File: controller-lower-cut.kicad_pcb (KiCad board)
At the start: 2 copper layers, 76.3 x 77 mm, 72 parts, among them J10 Phoenix MPT, J11 MicroFit_2x04, J12 Phoenix MPT, J13 MicroFit_2x04, J14 Phoenix MPT, J15 JST_B2B-XH, J16 MicroFit_2x04, J17 MLX_1x03, J18 MLX_1x03, J19 Phoenix MPT, J2 Conn_01x022_Male, J3 KYCON_KPJX-4S-S, J4 MicroFit_2x02, J5 24V/5A OUT, J7 Phoenix MPT, J9 Phoenix MPT, K1 OJS-SH-124HMF, Q1 BC847, Q2 IRFR5305TRPBF, Q3 BC857, Q4 BC847, Q5 BC857, U1 MAX5035BUSA

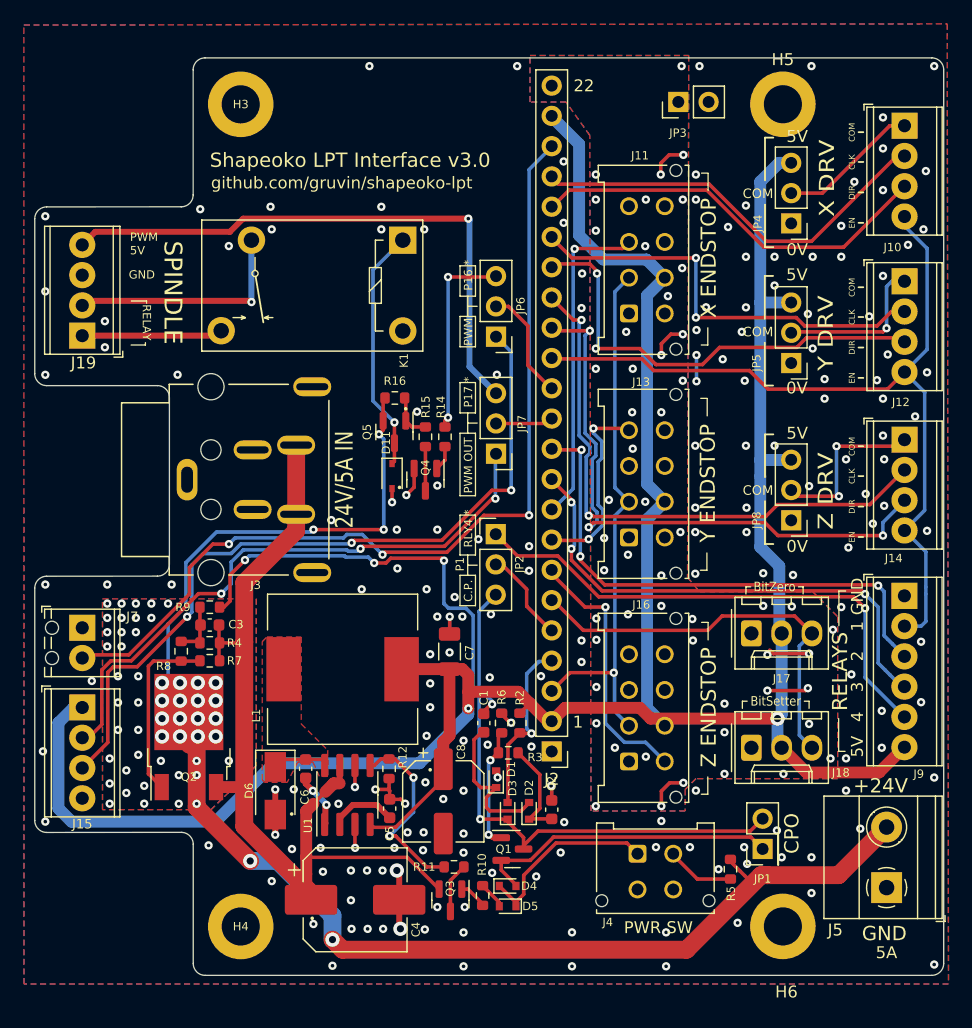
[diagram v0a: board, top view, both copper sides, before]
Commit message: v3.2 pre-production clean-up
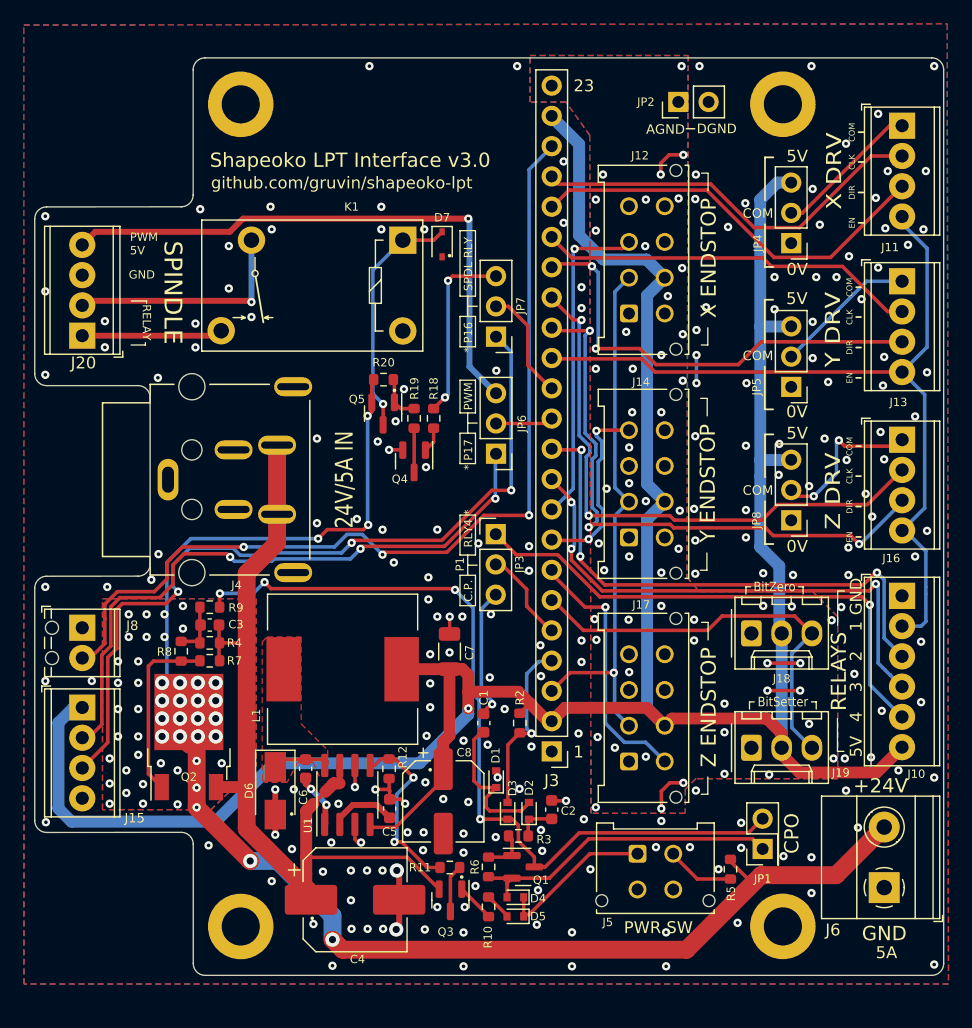
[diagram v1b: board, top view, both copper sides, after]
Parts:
- C1: value 10n/50V -> 100n/50V
- Q2: value IRFR5305TRPBF -> FDD5614P
- Q3: footprint Package_TO_SOT_SMD:SOT-23 -> -Project:SOT-23_DOT
- moved D7 19.9 mm to (70.9, 45.8)
- moved R6 12.1 mm to (74.8, 98.0), turned to -90 degrees
- moved R3 7.03 mm to (77.3, 95.4)
- moved JP5 2.00 mm to (100.2, 57.7)
- moved R20 1.81 mm to (66.0, 57.1)
- moved Q4 1.81 mm to (68.5, 64.0)
- moved Q5 1.81 mm to (66.0, 60.0)
- moved R18 1.81 mm to (70.2, 60.4)
- moved R19 1.81 mm to (68.5, 60.4)
- moved Q1 1.75 mm to (77.7, 98.0)
- moved JP4 1.66 mm to (100.2, 45.6)
- moved J4 1.60 mm to (57.0, 65.5)
- moved D4 1.15 mm to (77.0, 100.5), turned to 180 degrees
- moved R10 1.07 mm to (74.8, 101.3)
- moved D5 1.07 mm to (77.0, 102.2)
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- renumbered D11 to D7, H3 to H5, H4 to H6, H5 to H7, H6 to H8, J9 to J10, J10 to J11, J11 to J12, J12 to J13, J13 to J14, J14 to J16, J16 to J17, J17 to J18, J18 to J19, J19 to J20, J2 to J3, J3 to J4, J4 to J5, J5 to J6, J7 to J8, JP3 to JP2, JP2 to JP3, JP7 to JP6, JP6 to JP7, NT16 to NT22, NT17 to NT23, NT18 to NT24, NT33 to NT25, NT34 to NT26, NT35 to NT27, NT37 to NT28, R14 to R18, R15 to R19, R16 to R20
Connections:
- R6 pad 2: GND -> /Power/Q1_E
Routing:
- net /Power/Q1_B: track 10.2 -> 3.78 mm, vias 2 -> 0
- net Net-(C2-Pad1): track 8.61 -> 3.35 mm
- net GNDA: track 16.5 -> 12.3 mm, vias 53 -> 55
- net /Connectors & Jumpers/YCLK_IN: track 36.1 -> 32.0 mm, vias 2 -> 0
- net GND: track 27.4 -> 23.8 mm, vias 186 -> 199
- net /Connectors & Jumpers/X_P17_OUT: track 50.6 -> 53.6 mm
- net /Power/Q1_C: track 72.9 -> 70.0 mm
- net /Connectors & Jumpers/X_P16_OUT: track 64.8 -> 67.6 mm
- net Net-(D4-Pad1): track 16.2 -> 13.4 mm
- net +5V: track 174.5 -> 177.1 mm, vias 2 -> 1
- net /Connectors & Jumpers/STP_5V: track 31.8 -> 30.3 mm
- net /Connectors & Jumpers/RELAY3_IN: track 40.5 -> 42.0 mm
- net /Connectors & Jumpers/ESTOP_OUT: track 76.9 -> 78.3 mm
- net /Connectors & Jumpers/Y_COM: track 13.4 -> 11.9 mm, vias 1 -> 0
- net /Connectors & Jumpers/RELAY2_IN: track 42.5 -> 43.9 mm
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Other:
- outline, holes or cut-outs redrawn
- board text added: "* P16"
- board text added: "* P17"
- board text added: "23"
- board text added: "AGND"
- board text added: "DGND"
- board text added: "SPDL RLY"
- board text removed: "22"
- board text removed: "C"
- board text removed: "P16 *"
- board text removed: "P17 *"
- board text removed: "PWM OUT"
- board text removed: "TOOLING HOLE 1/3"

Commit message: more clean-up
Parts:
- moved J18 0.15 mm to (96.7, 78.4)
- moved J19 0.15 mm to (96.7, 88.0)
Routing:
- net GND: track 23.8 -> 21.4 mm, vias 199 -> 197
- net /Connectors & Jumpers/P16_IN: track 9.49 -> 8.81 mm
- net /Connectors & Jumpers/ZDIR_IN: track 49.7 -> 49.1 mm
- net GNDA: track 12.3 -> 12.8 mm, vias 55 -> 56
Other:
- board text added: "C"
- board text added: "Shapeoko LPT Interface v3.2"
- board text removed: "Shapeoko LPT Interface v3.0"

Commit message: more clean-up
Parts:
- added C10: 100n/50V, Capacitor_SMD:C_0603_1608Metric, F.Cu at (66.5, 127.8)
- added C11: 100n/50V, Capacitor_SMD:C_0603_1608Metric, F.Cu at (77.8, 144.4)
- added C12: 100n/50V, Capacitor_SMD:C_0603_1608Metric, F.Cu at (76.4, 127.7)
- added C9: 100n/50V, Capacitor_SMD:C_0603_1608Metric, F.Cu at (66.4, 159.1)
- added H1: MountingHole_Pad, MountingHole:MountingHole_3.2mm_M3_ISO14580_Pad, F.Cu at (110.0, 120.0)
- added H2: MountingHole_Pad, MountingHole:MountingHole_3.2mm_M3_ISO14580_Pad, F.Cu at (110.0, 189.0)
- added H3: MountingHole_Pad, MountingHole:MountingHole_3.2mm_M3_ISO14580_Pad, F.Cu at (54.0, 120.0)
- added H4: MountingHole_Pad, MountingHole:MountingHole_3.2mm_M3_ISO14580_Pad, F.Cu at (54.0, 189.0)
- added J1: Conn_01x06_Female, Connector_PinSocket_2.54mm:PinSocket_1x23_P2.54mm_Vertical, B.Cu at (136.1, 174.4)
- added J2: Conn_01x06_Female, Connector_PinSocket_2.54mm:PinSocket_1x23_P2.54mm_Vertical, B.Cu at (80.1, 174.4)
- added J7: DB25 FEMALE, Connector_Dsub:DSUB-25_Male_Horizontal_P2.77x2.84mm_EdgePinOffset7.70mm_Housed_MountingHolesOffset9.12mm, F.Cu at (55.6, 137.9)
- added NT1: NetTie_2, -Project:NetTie-2_SMD_Pad0.3mm, F.Cu at (74.6, 171.9)
- added R13: 1M, Resistor_SMD:R_0603_1608Metric, F.Cu at (73.3, 172.8)
- added R14: 330, Resistor_SMD:R_0603_1608Metric, F.Cu at (76.5, 167.2)
- added R15: 330, Resistor_SMD:R_0603_1608Metric, F.Cu at (76.5, 164.7)
- added R16: 330, Resistor_SMD:R_0603_1608Metric, F.Cu at (76.5, 162.2)
- added R17: 330, Resistor_SMD:R_0603_1608Metric, F.Cu at (76.5, 159.6)
- added R22: 330, Resistor_SMD:R_0603_1608Metric, F.Cu at (76.8, 121.5)
- added RN1: 1Kx4, Resistor_SMD:R_Array_Convex_4x0603, F.Cu at (64.6, 165.0)
- added RN2: 1Kx4, Resistor_SMD:R_Array_Convex_4x0603, F.Cu at (64.9, 123.1)
- added U2: 74HC245, Package_SO:SOIC-20W_7.5x12.8mm_P1.27mm, F.Cu at (71.2, 136.2)
- added U3: 74HC245, Package_SO:SOIC-20W_7.5x12.8mm_P1.27mm, F.Cu at (71.0, 150.8)
- added U4: ACSL-6310, Package_SO:SO-16_3.9x9.9mm_P1.27mm, F.Cu at (71.1, 164.0)
- added U5: ACSL-6310, Package_SO:SO-16_3.9x9.9mm_P1.27mm, F.Cu at (71.1, 123.3)
- added U6: USBLC6-2SC6, Package_TO_SOT_SMD:SOT-23-6, F.Cu at (111.0, 177.5)
- added U7: ADUM4160, Package_SO:SOIC-16W_7.5x10.3mm_P1.27mm, F.Cu at (114.8, 169.3)
- added U8: ATmega16U2-A, Package_QFP:TQFP-32_7x7mm_P0.8mm, F.Cu at (127.1, 169.2)
- added U9: ATmega328P-A, Package_QFP:TQFP-32_7x7mm_P0.8mm, F.Cu at (120.8, 150.9)
- JP1: value Jumper_2_Bridged -> Jumper_2
- JP4, JP5, JP8: value Jumper_3_Open -> Jumper_3
- moved R12 0.10 mm to (66.5, 89.8)
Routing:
- net +5VA: track 0.00 -> 179.6 mm, vias 0 -> 3
- net /LPT Interface/P1_IN: track 0.00 -> 63.5 mm, vias 0 -> 1
- net /LPT Interface/nCE_IN: track 0.00 -> 45.1 mm, vias 0 -> 4
- net GND2: track 0.00 -> 42.3 mm, vias 0 -> 44
- net /LPT Interface/P15_OUT: track 0.00 -> 28.3 mm
- net /LPT Interface/P7_IN: track 0.00 -> 23.0 mm
- net /LPT Interface/P6_IN: track 0.00 -> 21.1 mm
- net /LPT Interface/P5_IN: track 0.00 -> 19.3 mm
- net /LPT Interface/P4_IN: track 0.00 -> 17.5 mm
- net /LPT Interface/P3_IN: track 0.00 -> 15.7 mm
- net /LPT Interface/P11_OUT: track 0.00 -> 15.6 mm
- net /LPT Interface/P13_OUT: track 0.00 -> 15.5 mm
- net /LPT Interface/P9_IN: track 0.00 -> 15.4 mm, vias 0 -> 1
- net /LPT Interface/P12_OUT: track 0.00 -> 15.3 mm
- net GND1: track 0.00 -> 15.3 mm, vias 0 -> 77
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- added copper zone on B.Cu, net GND1
- added copper zone on F.Cu, net GND1
- added copper zone on B.Cu, net GND2
- added copper zone on F.Cu, net GND2
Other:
- board size 76.3 x 77 mm -> 101.3 x 162.9 mm
- board text added: "(JP3)"
- board text added: "10"
- board text added: "11"
- board text added: "12"
- board text added: "13"
- board text added: "5"
- board text added: "6"
- board text added: "7"
- board text added: "8"
- board text added: "9"
- board text added: "ES"
- board text added: "LPT INTERFACE"
- board text added: "PROBE"
- board text added: "RLY2"
- board text added: "RLY3"
- board text added: "RLY4/CP"
- board text added: "USB GRBL INTERFACE"
- board text added: "XMIN"
- board text added: "YCLK"
- board text added: "YMIN"
- board text added: "ZCLK"
- board text added: "ZMIN"

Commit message: commit to v3.2 production
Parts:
- removed C10, C11, C12, C9: 100n/50V, Capacitor_SMD:C_0603_1608Metric
- removed H1, H2, H3, H4: MountingHole_Pad, MountingHole:MountingHole_3.2mm_M3_ISO14580_Pad
- removed J1, J2: Conn_01x06_Female, Connector_PinSocket_2.54mm:PinSocket_1x23_P2.54mm_Vertical
- removed J7: DB25 FEMALE, Connector_Dsub:DSUB-25_Male_Horizontal_P2.77x2.84mm_EdgePinOffset7.70mm_Housed_MountingHolesOffset9.12mm
- removed NT1: NetTie_2, -Project:NetTie-2_SMD_Pad0.3mm
- removed R13: 1M, Resistor_SMD:R_0603_1608Metric
- removed R14, R15, R16, R17, R22: 330, Resistor_SMD:R_0603_1608Metric
- removed RN1, RN2: 1Kx4, Resistor_SMD:R_Array_Convex_4x0603
- removed U2, U3: 74HC245, Package_SO:SOIC-20W_7.5x12.8mm_P1.27mm
- removed U4, U5: ACSL-6310, Package_SO:SO-16_3.9x9.9mm_P1.27mm
- removed U6: USBLC6-2SC6, Package_TO_SOT_SMD:SOT-23-6
- removed U7: ADUM4160, Package_SO:SOIC-16W_7.5x10.3mm_P1.27mm
- removed U8: ATmega16U2-A, Package_QFP:TQFP-32_7x7mm_P0.8mm
- removed U9: ATmega328P-A, Package_QFP:TQFP-32_7x7mm_P0.8mm
- moved C5 0.49 mm to (66.5, 93.6)
- moved R12 0.49 mm to (66.5, 90.2)
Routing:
- net +5VA: track 179.6 -> 0.00 mm, vias 3 -> 0
- net /LPT Interface/P1_IN: track 63.5 -> 0.00 mm, vias 1 -> 0
- net /LPT Interface/nCE_IN: track 45.1 -> 0.00 mm, vias 4 -> 0
- net GND2: track 42.3 -> 0.00 mm, vias 44 -> 0
- net /LPT Interface/P15_OUT: track 28.3 -> 0.00 mm
- net /LPT Interface/P7_IN: track 23.0 -> 0.00 mm
- net /LPT Interface/P6_IN: track 21.1 -> 0.00 mm
- net /LPT Interface/P5_IN: track 19.3 -> 0.00 mm
- net /LPT Interface/P4_IN: track 17.5 -> 0.00 mm
- net /LPT Interface/P3_IN: track 15.7 -> 0.00 mm
- net /LPT Interface/P11_OUT: track 15.6 -> 0.00 mm
- net /LPT Interface/P13_OUT: track 15.5 -> 0.00 mm
- net /LPT Interface/P9_IN: track 15.4 -> 0.00 mm, vias 1 -> 0
- net /LPT Interface/P12_OUT: track 15.3 -> 0.00 mm
- net GND1: track 15.3 -> 0.00 mm, vias 77 -> 0
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- removed copper zone on B.Cu, net GND1
- removed copper zone on F.Cu, net GND1
- removed copper zone on B.Cu, net GND2
- removed copper zone on F.Cu, net GND2
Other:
- board size 101.3 x 162.9 mm -> 76.3 x 77 mm
- board text removed: "(JP3)"
- board text removed: "10"
- board text removed: "11"
- board text removed: "12"
- board text removed: "13"
- board text removed: "5"
- board text removed: "6"
- board text removed: "7"
- board text removed: "8"
- board text removed: "9"
- board text removed: "C"
- board text removed: "ES"
- board text removed: "LPT INTERFACE"
- board text removed: "PROBE"
- board text removed: "RLY2"
- board text removed: "RLY3"
- board text removed: "RLY4/CP"
- board text removed: "USB GRBL INTERFACE"
- board text removed: "XMIN"
- board text removed: "YCLK"
- board text removed: "YMIN"
- board text removed: "ZCLK"
- board text removed: "ZMIN"
